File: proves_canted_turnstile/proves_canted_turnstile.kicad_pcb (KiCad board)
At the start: 4 copper layers, 100 x 100 mm, 21 parts, among them J1 Conn_Coaxial, U1 QBA-07+, U2 QBA-07+, U3 QBA-07+

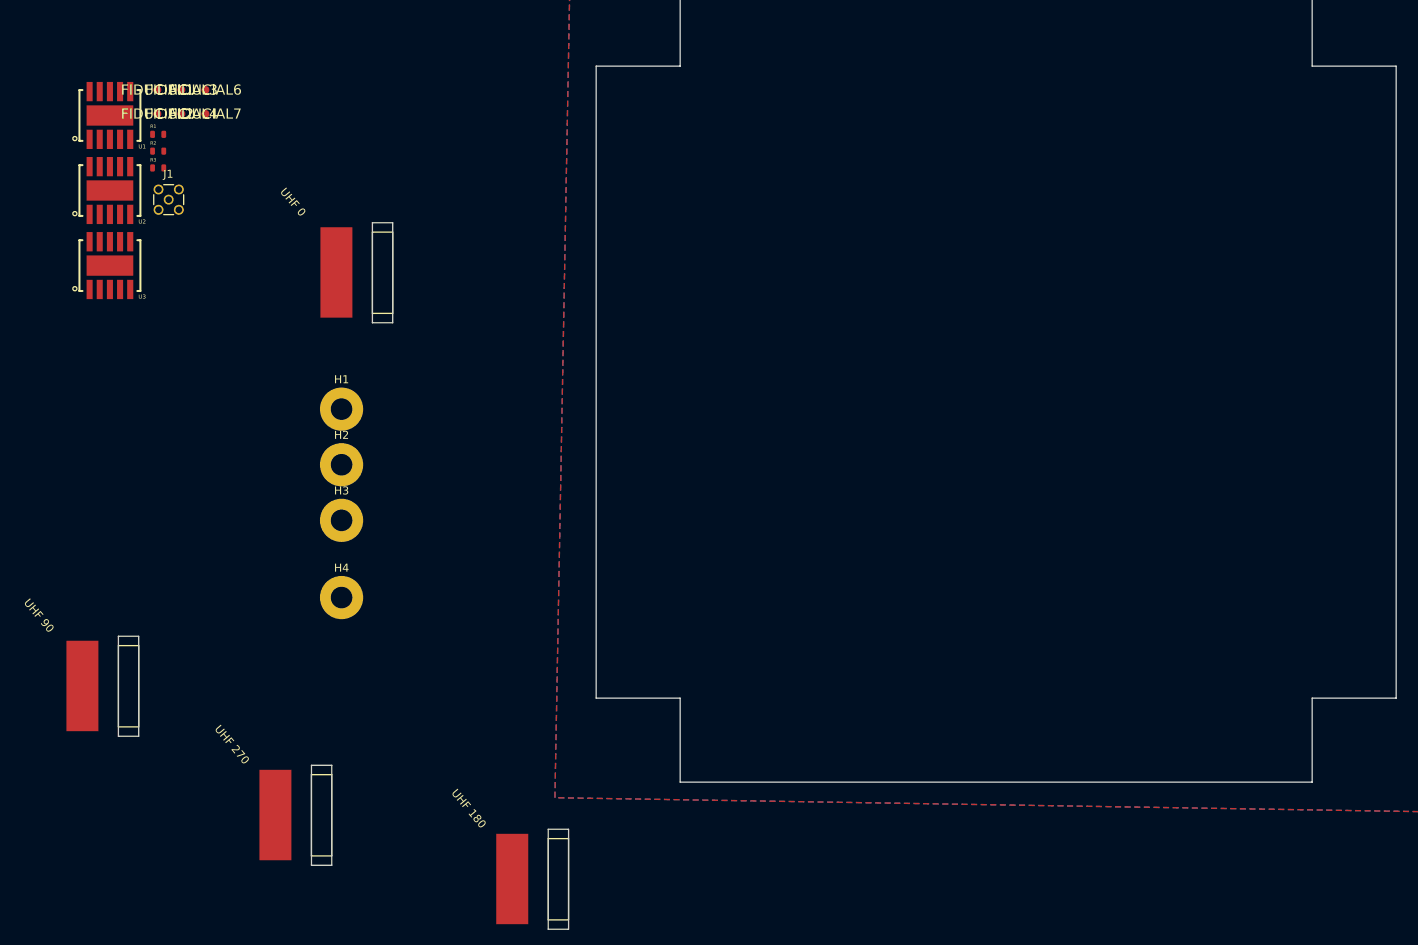
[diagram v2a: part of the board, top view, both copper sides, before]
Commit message: implemented burnwire in schematic
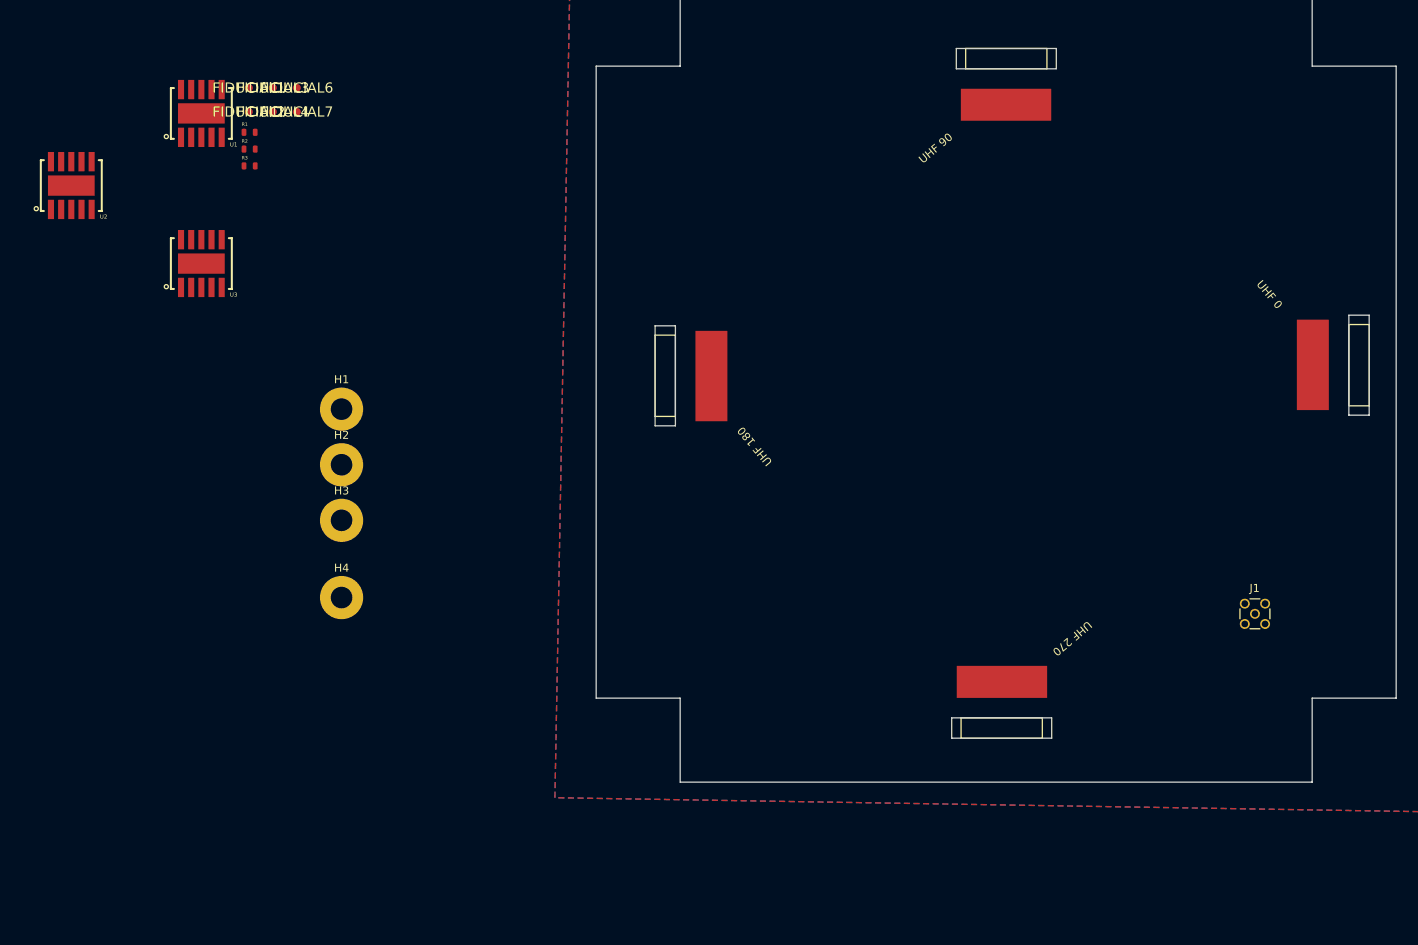
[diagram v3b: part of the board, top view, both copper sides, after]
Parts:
- moved J1 145.3 mm to (193.7, 119.9)
- moved UHF 0 122.6 mm to (200.5, 78.4)
- moved UHF 90 122.3 mm to (152.2, 56.7), turned to 90 degrees
- moved UHF 270 101.9 mm to (172.4, 127.9), turned to -90 degrees
- moved UHF 180 49.4 mm to (126.2, 100.6), turned to 180 degrees
- moved FIDUCIAL1 11.4 mm to (67.9, 54.1)
- moved FIDUCIAL2 11.4 mm to (67.9, 57.1)
- moved FIDUCIAL3 11.4 mm to (70.9, 54.1)
- moved FIDUCIAL4 11.4 mm to (70.9, 57.1)
- moved FIDUCIAL6 11.4 mm to (73.9, 54.1)
- moved FIDUCIAL7 11.4 mm to (73.9, 57.1)
- moved U3 11.4 mm to (62.0, 76.1)
- moved U1 11.4 mm to (62.0, 57.3)
- moved R2 11.4 mm to (68.0, 61.8)
- moved R3 11.4 mm to (68.0, 63.9)
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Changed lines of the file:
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@@
 	(footprint "Turnstile_Library:Singular_Tape_Measure_Antenna"
 		(layer "F.Cu")
-		(at 100.378001 142.649802)
+		(at 126.189999 100.555198 180)
 		(property "Reference" "UHF 180"
-			(at -4.967884 1.59847 310)
+			(at -4.967884 1.59847 130)
 			(unlocked yes)
 			(layer "F.SilkS")
@@
 		)
 		(property "Value" "Antenna"
-			(at 0 1.000001 0)
+			(at 0 1.000001 180)
 			(unlocked yes)
 			(layer "F.Fab")
@@
 		)
 		(property "Datasheet" "~"
-			(at 0 0 0)
+			(at 0 0 180)
 			(unlocked yes)
 			(layer "F.Fab")
@@
 		)
 		(property "Description" "Antenna"
-			(at 0 0 0)
+			(at 0 0 180)
 			(unlocked yes)
 			(layer "F.Fab")
@@
 		(attr smd)
 		(fp_line
-			(start 4.959999 15.499999)
-			(end 7.5 15.500001)
+			(start 7.5 15.500001)
+			(end 7.499999 5.34)
 			(stroke
 				(width 0.12)
@@
 		)
 		(fp_line
-			(start 4.96 5.339999)
-			(end 4.959999 15.499999)
+			(start 7.499999 5.34)
+			(end 4.96 5.339999)
 			(stroke
 				(width 0.12)
@@
 		)
 		(fp_line
-			(start 7.499999 5.34)
-			(end 4.96 5.339999)
+			(start 4.96 5.339999)
+			(end 4.959999 15.499999)
 			(stroke
 				(width 0.12)
@@
 		)
 		(fp_line
-			(start 7.5 15.500001)
-			(end 7.499999 5.34)
+			(start 4.959999 15.499999)
+			(end 7.5 15.500001)
 			(stroke
 				(width 0.12)
@@
 		)
 		(fp_line
-			(start 4.96 4.17)
-			(end 4.96 16.67)
+			(start 7.5 4.17)
+			(end 4.96 4.17)
 			(stroke
 				(width 0.05)
@@
 		)
 		(fp_line
-			(start 4.96 16.67)
-			(end 7.499999 16.669999)
+			(start 7.499999 16.669999)
+			(end 7.5 4.17)
 			(stroke
 				(width 0.05)
@@
 		)
 		(fp_line
-			(start 7.499999 16.669999)
-			(end 7.5 4.17)
+			(start 4.96 16.67)
+			(end 7.499999 16.669999)
 			(stroke
 				(width 0.05)
@@
 		)
 		(fp_line
-			(start 7.5 4.17)
-			(end 4.96 4.17)
+			(start 4.96 4.17)
+			(end 4.96 16.67)
 			(stroke
 				(width 0.05)
@@
 		)
 		(fp_text user "${REFERENCE}"
-			(at 0 2.5 0)
+			(at 0 2.5 180)
 			(unlocked yes)
 			(layer "F.Fab")
@@
 		)
 		(pad "1" smd rect
-			(at 0.459999 10.385198)
+			(at 0.459999 10.385198 180)
 			(size 4 11.3)
 			(layers "F.Cu" "F.Mask" "F.Paste")
@@
 	(footprint "plusz-end-card-with-turnstile-mezzanine-eagle-import:QBA-07+"
 		(layer "F.Cu")
-		(at 50.546 57.594)
+		(at 61.976 57.34)
 		(property "Reference" "U1"
 			(at 3.556 4.191 0)
@@
 	(footprint "plusz-end-card-with-turnstile-mezzanine-eagle-import:FIDUCIAL-1.0X2.0"
 		(layer "F.Cu")
-		(at 56.4775 57.4025)
+		(at 67.9075 57.1485)
 		(descr "Moderate Fiducial, 1.0 mm diameter with 2 mm mask clearance")
 		(property "Reference" "FIDUCIAL2"
@@
 	(footprint "plusz-end-card-with-turnstile-mezzanine-eagle-import:FIDUCIAL-1.0X2.0"
 		(layer "F.Cu")
-		(at 56.4775 54.4025)
+		(at 67.9075 54.1485)
 		(descr "Moderate Fiducial, 1.0 mm diameter with 2 mm mask clearance")
 		(property "Reference" "FIDUCIAL1"
@@
 	(footprint "plusz-end-card-with-turnstile-mezzanine-eagle-import:FIDUCIAL-1.0X2.0"
 		(layer "F.Cu")
-		(at 62.4775 54.4025)
+		(at 73.9075 54.1485)
 		(descr "Moderate Fiducial, 1.0 mm diameter with 2 mm mask clearance")
 		(property "Reference" "FIDUCIAL6"
@@
 	(footprint "plusz-end-card-with-turnstile-mezzanine-eagle-import:FIDUCIAL-1.0X2.0"
 		(layer "F.Cu")
-		(at 59.4775 57.4025)
+		(at 70.9075 57.1485)
 		(descr "Moderate Fiducial, 1.0 mm diameter with 2 mm mask clearance")
 		(property "Reference" "FIDUCIAL4"
@@
 	(footprint "plusz-end-card-with-turnstile-mezzanine-eagle-import:QBA-07+"
 		(layer "F.Cu")
-		(at 50.546 66.977)
+		(at 45.72 66.357)
 		(property "Reference" "U2"
 			(at 3.556 4.191 0)
@@
 	(footprint "plusz-end-card-with-turnstile-mezzanine-eagle-import:.0603-C-NOSILK"
 		(layer "F.Cu")
-		(at 56.5775 64.1525)
+		(at 68.0075 63.8985)
 		(descr "0603 (metric 1608) tight 'IPC-C' without silkscreen\nIn house package for minimum spacing based on IPC-7351B. This package is identical to 0603-C, but has its tPlace silkscreen layer removed.")
 		(property "Reference" "R3"
@@
 	(footprint "Connector_Coaxial:MMCX_Molex_73415-1471_Vertical"
 		(layer "F.Cu")
-		(at 57.8925 68.1175)
+		(at 193.675 119.888)
 		(descr "http://www.molex.com/pdm_docs/sd/734151471_sd.pdf")
 		(tags "Molex MMCX Coaxial Connector 50 ohms Female Jack Vertical THT")
@@
 	(footprint "plusz-end-card-with-turnstile-mezzanine-eagle-import:.0603-C-NOSILK"
 		(layer "F.Cu")
-		(at 56.5775 59.9525)
+		(at 68.0075 59.6985)
 		(descr "0603 (metric 1608) tight 'IPC-C' without silkscreen\nIn house package for minimum spacing based on IPC-7351B. This package is identical to 0603-C, but has its tPlace silkscreen layer removed.")
 		(property "Reference" "R1"
@@
 	(footprint "plusz-end-card-with-turnstile-mezzanine-eagle-import:FIDUCIAL-1.0X2.0"
 		(layer "F.Cu")
-		(at 59.4775 54.4025)
+		(at 70.9075 54.1485)
 		(descr "Moderate Fiducial, 1.0 mm diameter with 2 mm mask clearance")
 		(property "Reference" "FIDUCIAL3"
@@
 	(footprint "plusz-end-card-with-turnstile-mezzanine-eagle-import:FIDUCIAL-1.0X2.0"
 		(layer "F.Cu")
-		(at 62.4775 57.4025)
+		(at 73.9075 57.1485)
 		(descr "Moderate Fiducial, 1.0 mm diameter with 2 mm mask clearance")
 		(property "Reference" "FIDUCIAL7"
@@
 	(footprint "Turnstile_Library:Singular_Tape_Measure_Antenna"
 		(layer "F.Cu")
-		(at 46.647001 118.5235)
+		(at 152.174802 56.720999 90)
 		(property "Reference" "UHF 90"
-			(at -4.967884 1.59847 310)
+			(at -4.967884 1.59847 40)
 			(unlocked yes)
 			(layer "F.SilkS")
@@
 		)
 		(property "Value" "Antenna"
-			(at 0 1.000001 0)
+			(at 0 1.000001 90)
 			(unlocked yes)
 			(layer "F.Fab")
@@
 		)
 		(property "Datasheet" "~"
-			(at 0 0 0)
+			(at 0 0 90)
 			(unlocked yes)
 			(layer "F.Fab")
@@
 		)
 		(property "Description" "Antenna"
-			(at 0 0 0)
+			(at 0 0 90)
 			(unlocked yes)
 			(layer "F.Fab")
@@
 		(attr smd)
 		(fp_line
-			(start 4.959999 15.499999)
-			(end 7.5 15.500001)
+			(start 4.96 5.339999)
+			(end 4.959999 15.499999)
 			(stroke
 				(width 0.12)
@@
 		)
 		(fp_line
-			(start 4.96 5.339999)
-			(end 4.959999 15.499999)
+			(start 7.499999 5.34)
+			(end 4.96 5.339999)
 			(stroke
 				(width 0.12)
@@
 		)
 		(fp_line
-			(start 7.499999 5.34)
-			(end 4.96 5.339999)
+			(start 4.959999 15.499999)
+			(end 7.5 15.500001)
 			(stroke
 				(width 0.12)
@@
 		)
 		(fp_line
-			(start 4.96 4.17)
-			(end 4.96 16.67)
+			(start 7.5 4.17)
+			(end 4.96 4.17)
 			(stroke
 				(width 0.05)
@@
 		)
 		(fp_line
-			(start 4.96 16.67)
-			(end 7.499999 16.669999)
+			(start 4.96 4.17)
+			(end 4.96 16.67)
 			(stroke
 				(width 0.05)
@@
 		)
 		(fp_line
-			(start 7.5 4.17)
-			(end 4.96 4.17)
+			(start 4.96 16.67)
+			(end 7.499999 16.669999)
 			(stroke
 				(width 0.05)
@@
 		)
 		(fp_text user "${REFERENCE}"
-			(at 0 2.5 0)
+			(at 0 2.5 90)
 			(unlocked yes)
 			(layer "F.Fab")
@@
 		)
 		(pad "1" smd rect
-			(at 0.459999 10.385198)
+			(at 0.459999 10.385198 90)
 			(size 4 11.3)
 			(layers "F.Cu" "F.Mask" "F.Paste")
@@
 	(footprint "Turnstile_Library:Singular_Tape_Measure_Antenna"
 		(layer "F.Cu")
-		(at 70.777001 134.6525)
+		(at 172.437198 127.937001 -90)
 		(property "Reference" "UHF 270"
-			(at -4.967884 1.59847 310)
+			(at -4.967884 1.59847 220)
 			(unlocked yes)
 			(layer "F.SilkS")
@@
 		)
 		(property "Value" "Antenna"
-			(at 0 1.000001 0)
+			(at 0 1.000001 270)
 			(unlocked yes)
 			(layer "F.Fab")
@@
 		)
 		(property "Datasheet" "~"
-			(at 0 0 0)
+			(at 0 0 270)
 			(unlocked yes)
 			(layer "F.Fab")
@@
 		)
 		(property "Description" "Antenna"
-			(at 0 0 0)
+			(at 0 0 270)
 			(unlocked yes)
 			(layer "F.Fab")
@@
 		(attr smd)
 		(fp_line
-			(start 4.959999 15.499999)
-			(end 7.5 15.500001)
+			(start 7.5 15.500001)
+			(end 7.499999 5.34)
 			(stroke
 				(width 0.12)
@@
 		)
 		(fp_line
-			(start 4.96 5.339999)
-			(end 4.959999 15.499999)
+			(start 4.959999 15.499999)
+			(end 7.5 15.500001)
 			(stroke
 				(width 0.12)
@@
 		)
 		(fp_line
-			(start 7.5 15.500001)
-			(end 7.499999 5.34)
+			(start 4.96 5.339999)
+			(end 4.959999 15.499999)
 			(stroke
 				(width 0.12)
@@
 		)
 		(fp_line
-			(start 4.96 4.17)
-			(end 4.96 16.67)
+			(start 4.96 16.67)
+			(end 7.499999 16.669999)
 			(stroke
 				(width 0.05)
@@
 		)
 		(fp_line
-			(start 4.96 16.67)
-			(end 7.499999 16.669999)
+			(start 7.499999 16.669999)
+			(end 7.5 4.17)
 			(stroke
 				(width 0.05)
@@
 		)
 		(fp_line
-			(start 7.499999 16.669999)
-			(end 7.5 4.17)
+			(start 4.96 4.17)
+			(end 4.96 16.67)
 			(stroke
 				(width 0.05)
@@
 		)
 		(fp_text user "${REFERENCE}"
-			(at 0 2.5 0)
+			(at 0 2.5 270)
 			(unlocked yes)
 			(layer "F.Fab")
@@
 		)
 		(pad "1" smd rect
-			(at 0.459999 10.385198)
+			(at 0.459999 10.385198 270)
 			(size 4 11.3)
 			(layers "F.Cu" "F.Mask" "F.Paste")
@@
 	(footprint "plusz-end-card-with-turnstile-mezzanine-eagle-import:QBA-07+"
 		(layer "F.Cu")
-		(at 50.546 76.36)
+		(at 61.976 76.106)
 		(property "Reference" "U3"
 			(at 3.556 4.191 0)
@@
 	(footprint "plusz-end-card-with-turnstile-mezzanine-eagle-import:.0603-C-NOSILK"
 		(layer "F.Cu")
-		(at 56.5775 62.0525)
+		(at 68.0075 61.7985)
 		(descr "0603 (metric 1608) tight 'IPC-C' without silkscreen\nIn house package for minimum spacing based on IPC-7351B. This package is identical to 0603-C, but has its tPlace silkscreen layer removed.")
 		(property "Reference" "R2"
@@
 	(footprint "Turnstile_Library:Singular_Tape_Measure_Antenna"
 		(layer "F.Cu")
-		(at 78.397001 66.8345)
+		(at 200.454001 78.387802)
 		(property "Reference" "UHF 0"
 			(at -4.967884 1.59847 310)
